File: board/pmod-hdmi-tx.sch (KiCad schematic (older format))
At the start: 10 parts, among them P1 PMOD-Device-x2-Generic, U2 24AA01/24LC01B, U3 XC9140

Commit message: Mostly working schematic.
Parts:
- removed JP1: JUMPER, symbol JUMPER
- removed P1: PMOD-Device-x2-Generic, symbol PMOD-Device-x2-Generic
- removed P?: CONN_02X02, symbol CONN_02X02
- removed R17: 10k, Resistors_SMD:R_0402, symbol R
- removed U2: 24AA01/24LC01B, symbol 24AA01/24LC01B
- added C?: 2.2uF, symbol C
- added C?: 220n, symbol C_Small
- added P1: PMOD-CONN_6X2, symbol PMOD-CONN_6X2
- added R?, RDC1, RDE1, REQ0, REQ1, ROE1: 10k, symbol R
- added U32: REG710-DBV, symbol REG710-DBV
- renumbered U3 to U31
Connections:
- net labels added: HDMI_TX0_CEC, HDMI_TX0_CLK+, HDMI_TX0_D0+, HDMI_TX0_DCC_EN, HDMI_TX0_DDET, HDMI_TX0_EQ0, HDMI_TX0_EQ1, HDMI_TX0_HIZ_EN, HDMI_TX0_HPD, HDMI_TX0_SCL, HDMI_TX0_SDA, TX05V0, ~HDMI_TX0_OE
- net labels removed: +5V, VCC5V0
- wire segments 95 -> 91
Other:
- note added: "3.3V to 5V Voltage Booster\nLoad only *one* option\n"
- note added: "By default, EQ0 and EQ1\nare pulled to VCC\ngiving 6dB equalization"
- note added: "HDMI High Speed Signals\nPositive signals on Top Row\nNegative signals on Bottom Row"
- note added: "On PTX0\n - DET on Pin X\n - DDC on Pin X\n - EQ1 on Pin X\n - EQ0 on Pin X"
- note added: "On PTX0\n - SCL on Pin X\n - SDA on Pin X\n - CEC on Pin X\n - HPD on Pin X"
- note added: "Option 1\n"
- note added: "Option 2"
- note removed: "3.3V to 5V Voltage Booster"
- moved on the sheet: C6, C7, L1, R18, U31

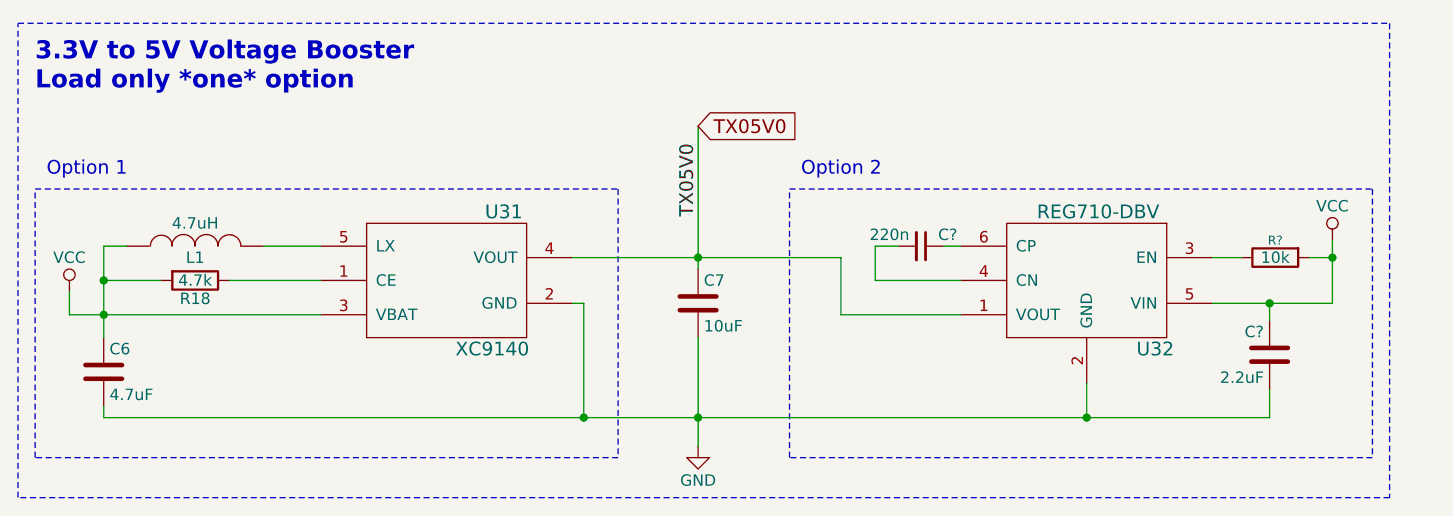
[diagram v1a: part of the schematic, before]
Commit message: Annotate schematic.
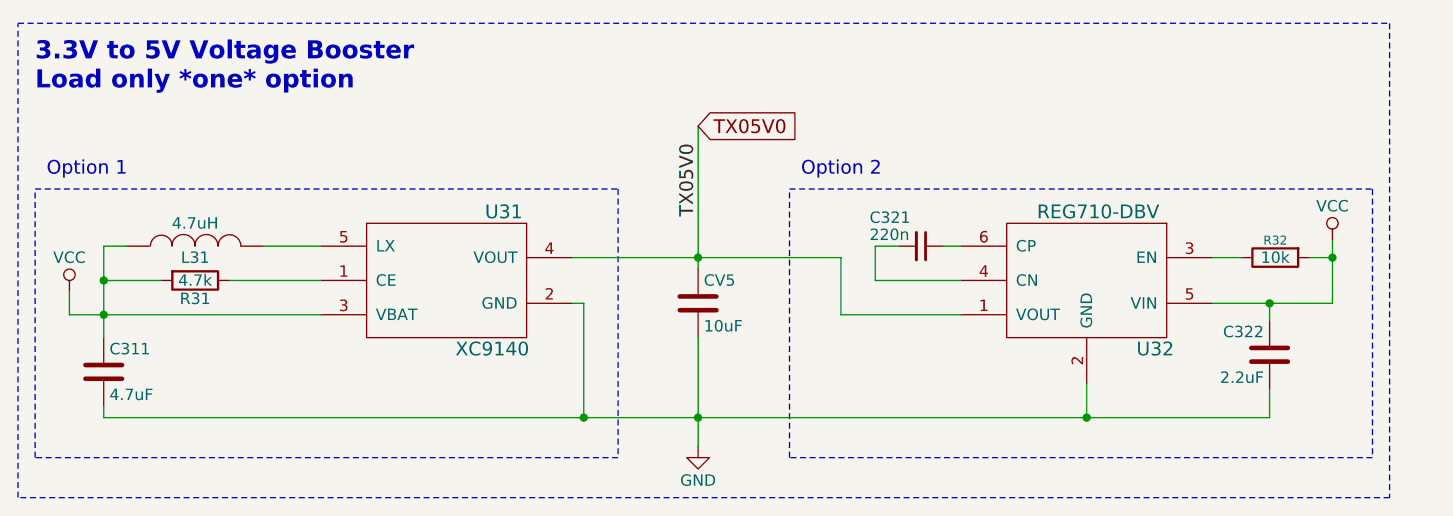
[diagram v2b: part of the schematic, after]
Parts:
- gave numbers to parts that had none: 3
- renumbered C6 to C311, C7 to CV5, L1 to L31, R18 to R31
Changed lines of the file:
@@
 encoding utf-8
 Sheet 1 2
-Title ""
+Title "PTN3363 HDMI Transmitter Expansion Module"
 Date ""
 Rev ""
-Comp ""
-Comment1 ""
-Comment2 ""
-Comment3 ""
-Comment4 ""
+Comp "https://github.com/mithro/pmod-hdmi-tx-ptn3363"
+Comment1 "Using references from Numato Lab and Apertus AXIOM"
+Comment2 "Designed by TimVideos.us"
+Comment3 "License: CC-BY-SA 4.0 International"
+Comment4 "$Id$"
 $EndDescr
 $Sheet
@@
 HDMI_TX0_CLK+
 $Comp
-L GND #PWR?
+L GND #PWR01
 U 1 1 58032FEA
 P 2500 3700
-F 0 "#PWR?" H 2500 3450 50  0001 C CNN
+F 0 "#PWR01" H 2500 3450 50  0001 C CNN
 F 1 "GND" H 2500 3550 50  0000 C CNN
 F 2 "" H 2500 3700 50  0000 C CNN
@@
 $EndComp
 $Comp
-L VCC #PWR?
+L VCC #PWR02
 U 1 1 5803306C
 P 2500 3450
-F 0 "#PWR?" H 2500 3300 50  0001 C CNN
+F 0 "#PWR02" H 2500 3300 50  0001 C CNN
 F 1 "VCC" H 2500 3600 50  0000 C CNN
 F 2 "" H 2500 3450 50  0000 C CNN
@@
 VCC3V3
 $Comp
-L VCC #PWR?
+L VCC #PWR03
 U 1 1 58037F54
 P 4700 1100
-F 0 "#PWR?" H 4700 950 50  0001 C CNN
+F 0 "#PWR03" H 4700 950 50  0001 C CNN
 F 1 "VCC" H 4700 1250 50  0000 C CNN
 F 2 "" H 4700 1100 50  0000 C CNN
@@
 $EndComp
 $Comp
-L INDUCTOR L1
+L INDUCTOR L31
 U 1 1 5803B5D8
 P 1350 6525
-F 0 "L1" V 1300 6525 50  0000 C CNN
+F 0 "L31" V 1300 6525 50  0000 C CNN
 F 1 "4.7uH" V 1450 6525 50  0000 C CNN
 F 2 "" H 1350 6525 50  0000 C CNN
@@
 $EndComp
 $Comp
-L R R18
+L R R31
 U 1 1 5803B7C8
 P 1350 6675
-F 0 "R18" V 1430 6675 50  0000 C CNN
+F 0 "R31" V 1430 6675 50  0000 C CNN
 F 1 "4.7k" V 1350 6675 50  0000 C CNN
 F 2 "" V 1280 6675 50  0000 C CNN
@@
 $EndComp
 $Comp
-L VCC #PWR?
+L VCC #PWR04
 U 1 1 5803BD68
 P 800 6725
-F 0 "#PWR?" H 800 6575 50  0001 C CNN
+F 0 "#PWR04" H 800 6575 50  0001 C CNN
 F 1 "VCC" H 800 6875 50  0000 C CNN
 F 2 "" H 800 6725 50  0000 C CNN
@@
 $EndComp
 $Comp
-L C C6
+L C C311
 U 1 1 5803BE39
 P 950 7075
-F 0 "C6" H 975 7175 50  0000 L CNN
+F 0 "C311" H 975 7175 50  0000 L CNN
 F 1 "4.7uF" H 975 6975 50  0000 L CNN
 F 2 "" H 988 6925 50  0000 C CNN
@@
 $EndComp
 $Comp
-L C C7
+L C CV5
 U 1 1 5803BFAE
 P 3550 6775
-F 0 "C7" H 3575 6875 50  0000 L CNN
+F 0 "CV5" H 3575 6875 50  0000 L CNN
 F 1 "10uF" H 3575 6675 50  0000 L CNN
 F 2 "" H 3588 6625 50  0000 C CNN
@@
 TX05V0
 $Comp
-L GND #PWR?
+L GND #PWR05
 U 1 1 5803DE38
 P 3550 7400
-F 0 "#PWR?" H 3550 7150 50  0001 C CNN
+F 0 "#PWR05" H 3550 7150 50  0001 C CNN
 F 1 "GND" H 3550 7250 50  0000 C CNN
 F 2 "" H 3550 7400 50  0000 C CNN
@@
 $EndComp
 $Comp
-L GND #PWR?
+L GND #PWR06
 U 1 1 5803760B
 P 7700 2425
-F 0 "#PWR?" H 7700 2175 50  0001 C CNN
+F 0 "#PWR06" H 7700 2175 50  0001 C CNN
 F 1 "GND" V 7700 2250 50  0000 C CNN
 F 2 "" H 7700 2425 50  0000 C CNN
@@
 $EndComp
 $Comp
-L GND #PWR?
+L GND #PWR07
 U 1 1 5803801E
 P 7700 2100
-F 0 "#PWR?" H 7700 1850 50  0001 C CNN
+F 0 "#PWR07" H 7700 1850 50  0001 C CNN
 F 1 "GND" V 7700 1925 50  0000 C CNN
 F 2 "" H 7700 2100 50  0000 C CNN
@@
 $EndComp
 $Comp
-L VCC #PWR?
+L VCC #PWR08
 U 1 1 58039EF2
 P 6600 3175
-F 0 "#PWR?" H 6600 3025 50  0001 C CNN
+F 0 "#PWR08" H 6600 3025 50  0001 C CNN
 F 1 "VCC" H 6600 3325 50  0000 C CNN
 F 2 "" H 6600 3175 50  0000 C CNN
@@
 $EndComp
 $Comp
-L VCC #PWR?
+L VCC #PWR09
 U 1 1 5803C0E2
 P 6325 6500
-F 0 "#PWR?" H 6325 6350 50  0001 C CNN
+F 0 "#PWR09" H 6325 6350 50  0001 C CNN
 F 1 "VCC" H 6325 6650 50  0000 C CNN
 F 2 "" H 6325 6500 50  0000 C CNN
@@
 $EndComp
 $Comp
-L C C?
+L C C322
 U 1 1 5803C17C
 P 6050 7000
-F 0 "C?" H 6075 7100 50  0000 L CNN
+F 0 "C322" H 6075 7100 50  0000 L CNN
 F 1 "2.2uF" H 6075 6900 50  0000 L CNN
 F 2 "" H 6088 6850 50  0000 C CNN
@@
 $EndComp
 $Comp
-L C_Small C?
+L C_Small C321
 U 1 1 5803CD16
 P 4525 6525
-F 0 "C?" V 4575 6600 50  0000 L CNN
+F 0 "C321" V 4650 6300 50  0000 L CNN
 F 1 "220n" V 4575 6300 50  0000 L CNN
 F 2 "" H 4525 6525 50  0000 C CNN
@@
 Option 2
 $Comp
-L R R?
+L R R32
 U 1 1 580409A1
 P 6075 6575
-F 0 "R?" V 6000 6575 39  0000 C CNN
+F 0 "R32" V 6000 6575 39  0000 C CNN
 F 1 "10k" V 6075 6575 50  0000 C CNN
 F 2 "" V 6005 6575 50  0000 C CNN

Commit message: Adding footprints.
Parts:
- C311, C322: footprint (none) -> Capacitors_SMD:C_0603
- C321: footprint (none) -> Capacitors_SMD:C_0402
- CV5: footprint (none) -> Capacitors_SMD:C_1206
- L31: footprint (none) -> Inductors_NEOSID:Neosid_Inductor_SM0603CG
- R31, R32, RDC1, RDE1, REQ0, REQ1, ROE1: footprint (none) -> Resistors_SMD:R_0402
- U31: footprint (none) -> TO_SOT_Packages_SMD:SOT-23-5
- U32: footprint (none) -> TO_SOT_Packages_SMD:SOT-23-6
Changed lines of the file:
@@
 F 0 "U31" H 2700 7475 60  0000 C CNN
 F 1 "XC9140" H 2650 6875 60  0000 C CNN
-F 2 "" H 2100 6925 60  0001 C CNN
+F 2 "TO_SOT_Packages_SMD:SOT-23-5" H 2100 6925 60  0001 C CNN
 F 3 "" H 2100 6925 60  0001 C CNN
 	1    2100 6925
@@
 F 0 "L31" V 1300 6525 50  0000 C CNN
 F 1 "4.7uH" V 1450 6525 50  0000 C CNN
-F 2 "" H 1350 6525 50  0000 C CNN
+F 2 "Inductors_NEOSID:Neosid_Inductor_SM0603CG" H 1350 6525 50  0001 C CNN
 F 3 "" H 1350 6525 50  0000 C CNN
 	1    1350 6525
@@
 F 0 "R31" V 1430 6675 50  0000 C CNN
 F 1 "4.7k" V 1350 6675 50  0000 C CNN
-F 2 "" V 1280 6675 50  0000 C CNN
+F 2 "Resistors_SMD:R_0402" V 1280 6675 50  0001 C CNN
 F 3 "" H 1350 6675 50  0000 C CNN
 	1    1350 6675
@@
 F 0 "C311" H 975 7175 50  0000 L CNN
 F 1 "4.7uF" H 975 6975 50  0000 L CNN
-F 2 "" H 988 6925 50  0000 C CNN
+F 2 "Capacitors_SMD:C_0603" H 988 6925 50  0001 C CNN
 F 3 "" H 950 7075 50  0000 C CNN
 	1    950  7075
@@
 F 0 "CV5" H 3575 6875 50  0000 L CNN
 F 1 "10uF" H 3575 6675 50  0000 L CNN
-F 2 "" H 3588 6625 50  0000 C CNN
+F 2 "Capacitors_SMD:C_1206" H 3588 6625 50  0001 C CNN
 F 3 "" H 3550 6775 50  0000 C CNN
 	1    3550 6775
@@
 F 0 "P1" H 2500 3300 60  0000 C CNN
 F 1 "PMOD-CONN_6X2" V 2500 2950 39  0000 C CNN
-F 2 "" H 2500 2950 60  0000 C CNN
+F 2 "" H 2500 2950 60  0001 C CNN
 F 3 "" H 2500 2950 60  0000 C CNN
 	1    2500 2950
@@
 F 0 "RDE1" V 7450 2000 39  0000 C CNN
 F 1 "10k" V 7425 2175 50  0000 C CNN
-F 2 "" V 7355 2175 50  0000 C CNN
+F 2 "Resistors_SMD:R_0402" V 7355 2175 50  0001 C CNN
 F 3 "" H 7425 2175 50  0000 C CNN
 	1    7425 2175
@@
 F 0 "RDC1" V 7450 2250 39  0000 C CNN
 F 1 "10k" V 7425 2425 50  0000 C CNN
-F 2 "" V 7355 2425 50  0000 C CNN
+F 2 "Resistors_SMD:R_0402" V 7355 2425 50  0001 C CNN
 F 3 "" H 7425 2425 50  0000 C CNN
 	1    7425 2425
@@
 F 0 "ROE1" V 7350 2000 39  0000 C CNN
 F 1 "10k" V 7425 2000 50  0000 C CNN
-F 2 "" V 7355 2000 50  0000 C CNN
+F 2 "Resistors_SMD:R_0402" V 7355 2000 50  0001 C CNN
 F 3 "" H 7425 2000 50  0000 C CNN
 	1    7425 2000
@@
 F 0 "REQ1" V 6800 3025 39  0000 C CNN
 F 1 "10k" V 6775 2825 50  0000 C CNN
-F 2 "" V 6705 2825 50  0000 C CNN
+F 2 "Resistors_SMD:R_0402" V 6705 2825 50  0001 C CNN
 F 3 "" H 6775 2825 50  0000 C CNN
 	1    6775 2825
@@
 F 0 "REQ0" V 6950 3025 39  0000 C CNN
 F 1 "10k" V 6925 2825 50  0000 C CNN
-F 2 "" V 6855 2825 50  0000 C CNN
+F 2 "Resistors_SMD:R_0402" V 6855 2825 50  0001 C CNN
 F 3 "" H 6925 2825 50  0000 C CNN
 	1    6925 2825
@@
 F 0 "U32" H 5650 6875 60  0000 C CNN
 F 1 "REG710-DBV" H 5900 7475 60  0000 C CNN
-F 2 "" H 5600 6925 60  0001 C CNN
+F 2 "TO_SOT_Packages_SMD:SOT-23-6" H 5600 6925 60  0001 C CNN
 F 3 "" H 5600 6925 60  0001 C CNN
 	1    5600 6925
@@
 F 0 "C322" H 6075 7100 50  0000 L CNN
 F 1 "2.2uF" H 6075 6900 50  0000 L CNN
-F 2 "" H 6088 6850 50  0000 C CNN
+F 2 "Capacitors_SMD:C_0603" H 6088 6850 50  0001 C CNN
 F 3 "" H 6050 7000 50  0000 C CNN
 	1    6050 7000
@@
 F 0 "C321" V 4650 6300 50  0000 L CNN
 F 1 "220n" V 4575 6300 50  0000 L CNN
-F 2 "" H 4525 6525 50  0000 C CNN
+F 2 "Capacitors_SMD:C_0402" H 4525 6525 50  0001 C CNN
 F 3 "" H 4525 6525 50  0000 C CNN
 	1    4525 6525
@@
 F 0 "R32" V 6000 6575 39  0000 C CNN
 F 1 "10k" V 6075 6575 50  0000 C CNN
-F 2 "" V 6005 6575 50  0000 C CNN
+F 2 "Resistors_SMD:R_0402" V 6005 6575 50  0001 C CNN
 F 3 "" H 6075 6575 50  0000 C CNN
 	1    6075 6575

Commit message: Assigning footprints.
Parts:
- P1: footprint (none) -> pmod:pmod_pin_array_6x2
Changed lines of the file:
@@
 F 0 "P1" H 2500 3300 60  0000 C CNN
 F 1 "PMOD-CONN_6X2" V 2500 2950 39  0000 C CNN
-F 2 "" H 2500 2950 60  0001 C CNN
+F 2 "pmod:pmod_pin_array_6x2" H 2500 2950 60  0001 C CNN
 F 3 "" H 2500 2950 60  0000 C CNN
 	1    2500 2950

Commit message: Update from templates + s/HPD/HOT/ + s/HPA/HOT/
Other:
- note added: "On PTX0\n - SCL on Pin X\n - SDA on Pin X\n - CEC on Pin X\n - HOT on Pin X"
- note removed: "On PTX0\n - SCL on Pin X\n - SDA on Pin X\n - CEC on Pin X\n - HPD on Pin X"
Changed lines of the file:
@@
 F15 "HDMI_TX0_SDA" B R 6250 1600 60
 F16 "HDMI_TX0_DDET" I R 6250 2250 60
-F17 "HDMI_TX0_HPD" O R 6250 1800 60
+F17 "HDMI_TX0_HOT" O R 6250 1800 60
 F18 "HDMI_TX0_HIZ_EN" I R 6250 2100 60
 F19 "HDMI_TX0_CEC" I R 6250 1700 60
@@
 HDMI_TX0_CEC
 Text Label 8125 1800 0    60   ~ 0
-HDMI_TX0_HPD
+HDMI_TX0_HOT
 Text Notes 8875 1850 0    60   ~ 0
-On PTX0\n - SCL on Pin X\n - SDA on Pin X\n - CEC on Pin X\n - HPD on Pin X
+On PTX0\n - SCL on Pin X\n - SDA on Pin X\n - CEC on Pin X\n - HOT on Pin X
 Text Notes 1850 4200 0    60   ~ 0
 HDMI High Speed Signals\nPositive signals on Top Row\nNegative signals on Bottom Row

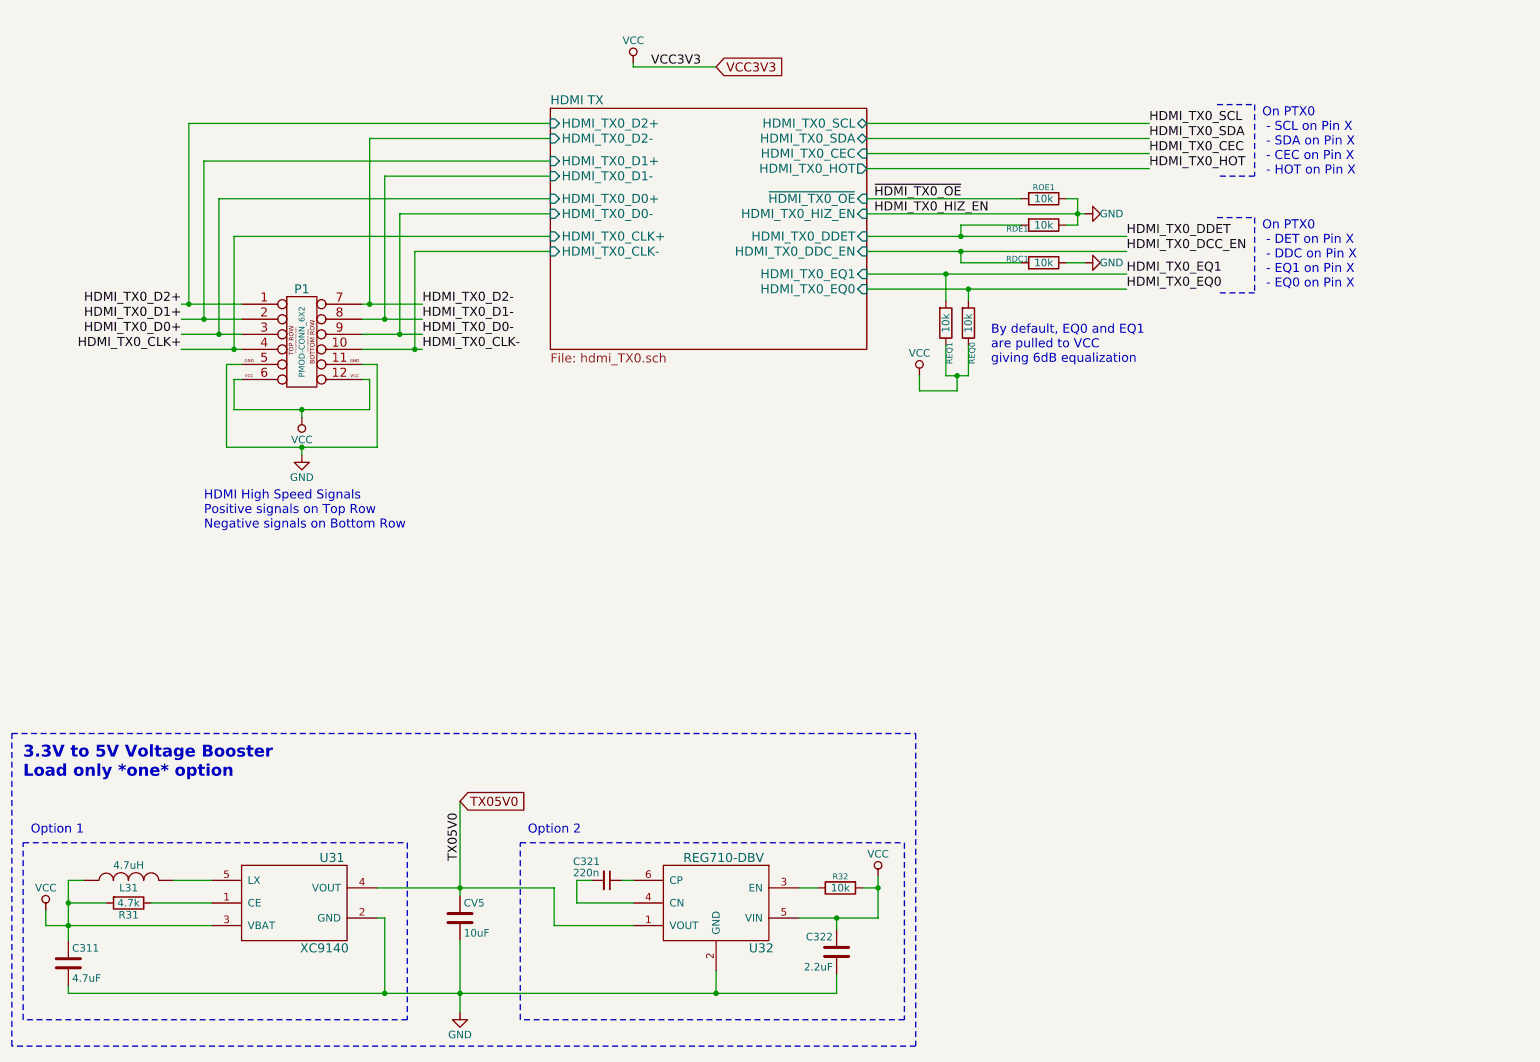
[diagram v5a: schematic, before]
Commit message: Changing how the high speed signals are routed.
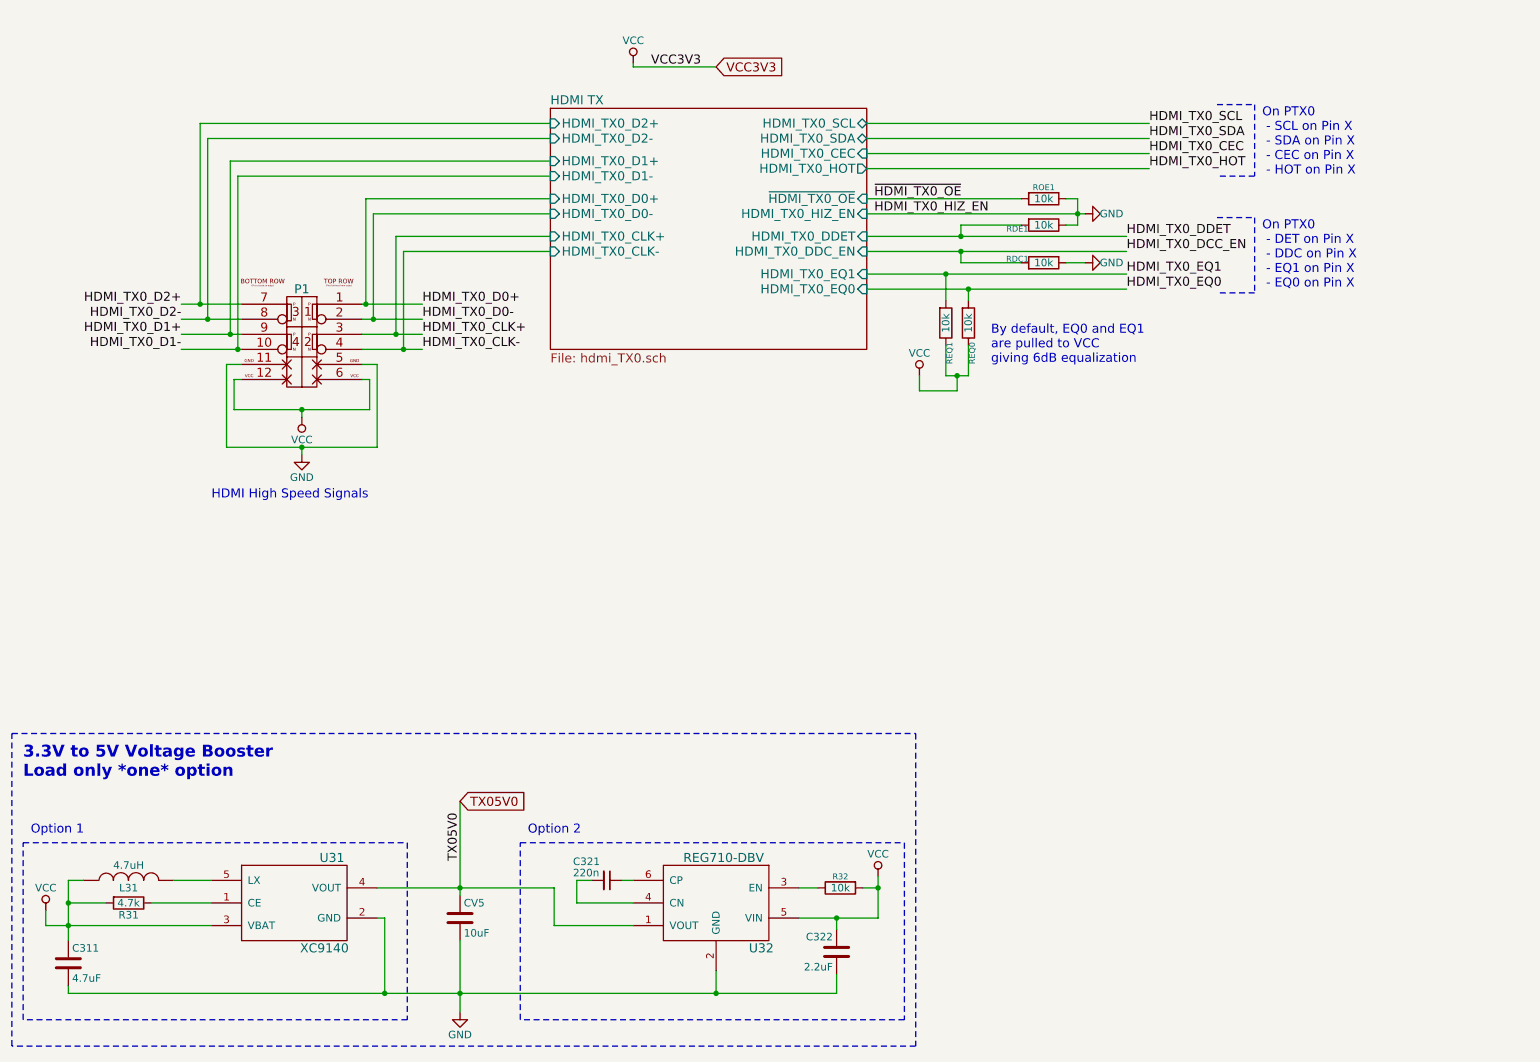
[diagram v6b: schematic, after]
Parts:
- removed P1: PMOD-CONN_6X2, pmod:pmod_pin_array_6x2, symbol PMOD-CONN_6X2
- added P1: PMOD-Device-x2-Type-XHS-Alt, pmod-conn_6x2:pmod_pin_array_6x2, symbol PMOD-Device-x2-Type-XHS-Alt
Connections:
- net GND: now also P1.11 (P11), P1.5 (P5)
- net HDMI_TX0_CLK+: now also P1.3 (JA2_P)
- net HDMI_TX0_CLK-: now also P1.4 (JA2_N)
- net HDMI_TX0_D0+: now also P1.1 (JA1_P)
- net HDMI_TX0_D0-: now also P1.2 (JA1_N)
- net HDMI_TX0_D1+: now also P1.9 (JA4_P)
- net HDMI_TX0_D1-: now also P1.10 (JA4_N)
- net HDMI_TX0_D2+: now also P1.7 (JA3_P)
- net HDMI_TX0_D2-: now also P1.8 (JA3_N)
- net VCC: now also P1.12 (P12), P1.6 (P6)
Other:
- note added: "HDMI High Speed Signals"
- note removed: "HDMI High Speed Signals\nPositive signals on Top Row\nNegative signals on Bottom Row"
